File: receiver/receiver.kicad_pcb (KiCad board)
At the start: 4 copper layers, 20.2 x 28 mm, 22 parts, among them J1 CONN_04SCREW, U1 10118194-MICRO-USB, U2 LM3671MF-3.3/NOPBMF05A-M, U3 SN74LVC2T45DCTRE4, U5 FT231XQ-R, U6 MBT3904DW1T1G

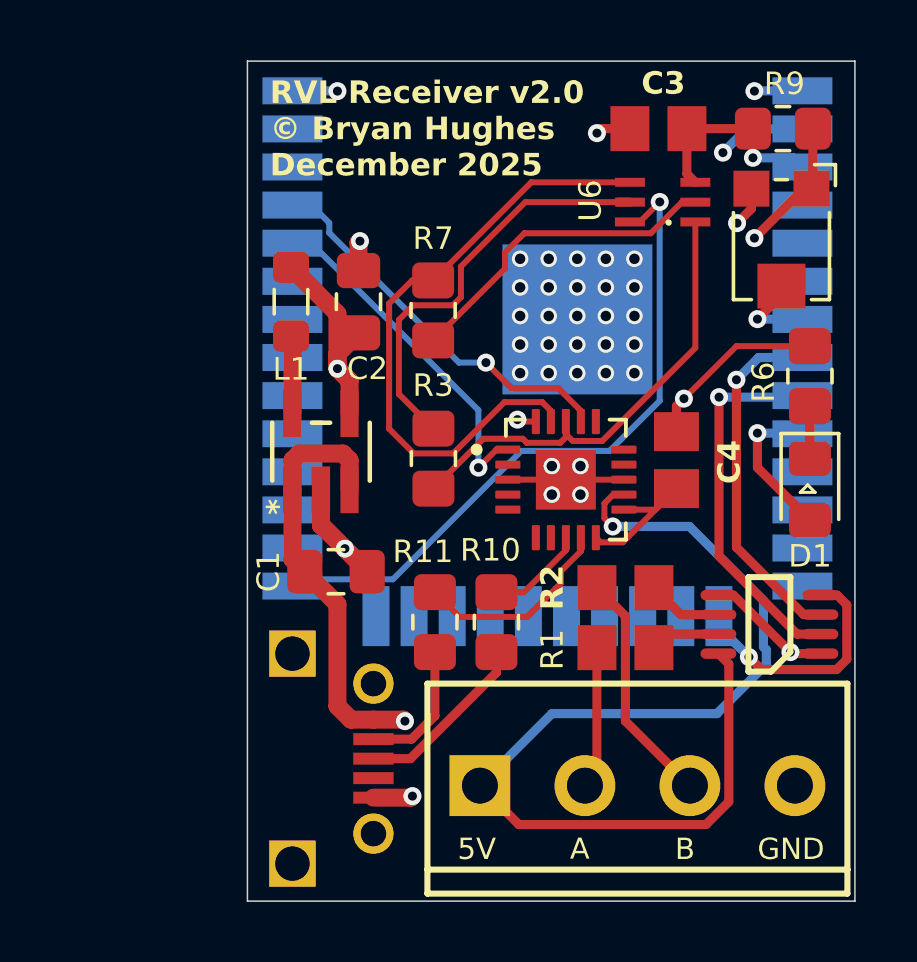
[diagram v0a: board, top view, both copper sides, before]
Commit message: restored v1.7 of receiver, since 2.0 is abandoned
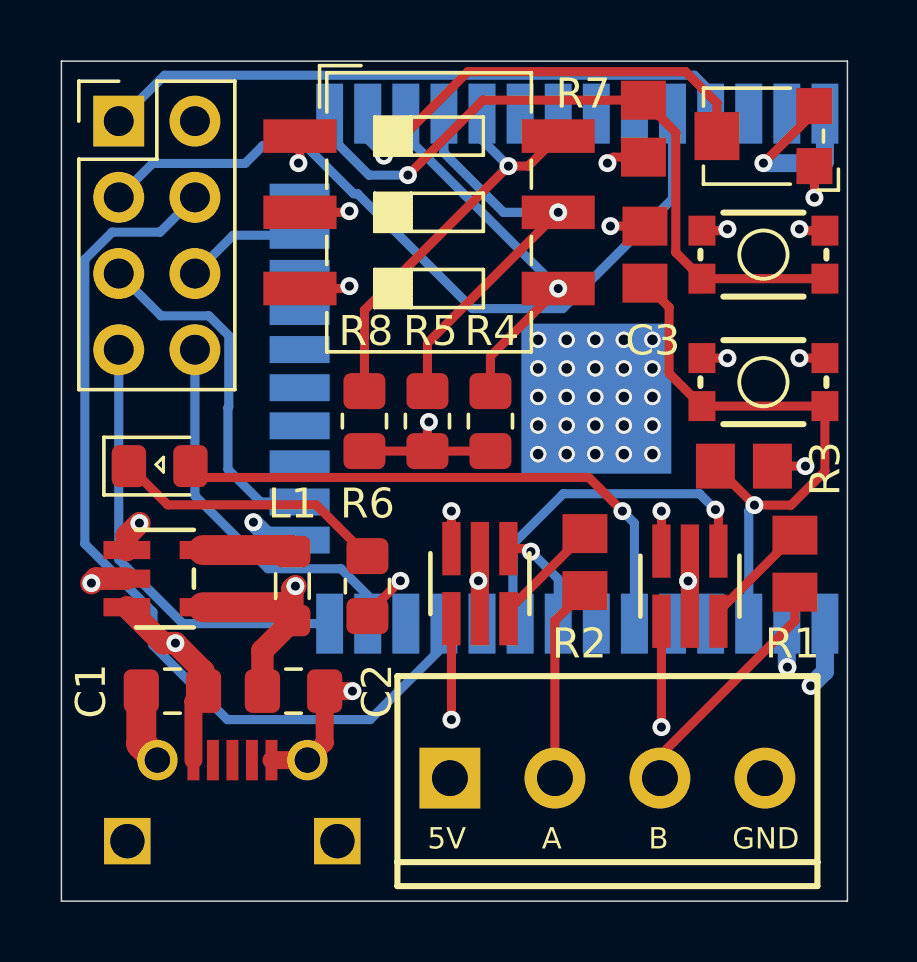
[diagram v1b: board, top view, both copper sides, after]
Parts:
- removed C4: 1uF, receiver:C0805
- removed D1: LED, LED_SMD:LED_0805_2012Metric_Pad1.15x1.40mm_HandSolder
- removed R10, R11: 27, Resistor_SMD:R_0805_2012Metric_Pad1.20x1.40mm_HandSolder
- removed R9: 10k, Resistor_SMD:R_0805_2012Metric_Pad1.20x1.40mm_HandSolder
- removed U5: FT231XQ-R, receiver:QFN50P400X400X80-21N
- removed U6: MBT3904DW1T1G, receiver:SOT236
- added J2: Conn_02x05_Counter_Clockwise, Connector_PinHeader_2.54mm:PinHeader_2x04_P2.54mm_Vertical, F.Cu at (98.7, 116.0)
- added LED1: Power, LED_SMD:LED_0805_2012Metric_Pad1.15x1.40mm_HandSolder, F.Cu at (100.1, 127.5)
- added R4: 10k, Resistor_SMD:R_0805_2012Metric_Pad1.20x1.40mm_HandSolder, F.Cu at (111.1, 126.0)
- added R5: 10k, Resistor_SMD:R_0805_2012Metric_Pad1.20x1.40mm_HandSolder, F.Cu at (109.0, 126.0)
- added R8: 10k, Resistor_SMD:R_0805_2012Metric_Pad1.20x1.40mm_HandSolder, F.Cu at (106.9, 126.0)
- added S2: MOMENTARY-SWITCH-SPST-2-SMD-4.6X2.8MM, receiver:TACTILE_SWITCH_SMD_4.6X2.8MM, F.Cu at (120.2, 120.5)
- added S3: MOMENTARY-SWITCH-SPST-2-SMD-4.6X2.8MM, receiver:TACTILE_SWITCH_SMD_4.6X2.8MM, F.Cu at (120.2, 124.7)
- added SW1: SW_DIP_x03, Button_Switch_SMD:SW_DIP_SPSTx03_Slide_6.7x9.18mm_W8.61mm_P2.54mm_LowProfile, F.Cu at (109.1, 119.0)
- added U4: SN74LVC1T45DBVRDBV6-M, receiver:DBV6-M, F.Cu at (110.8, 131.4)
- R3, R7: footprint Resistor_SMD:R_0805_2012Metric_Pad1.20x1.40mm_HandSolder -> receiver:R0805
- U3: value SN74LVC2T45DCTRE4 -> SN74LVC1T45DBVRDBV6-M; footprint receiver:DCT0008A_L -> receiver:DBV6-M
- moved R6 16.3 mm to (107.0, 131.5), turned to 90 degrees
- moved C2 13.2 mm to (104.5, 135.0), turned to 0 degrees
- moved U$2 13.1 mm to (122.2, 124.2), turned to 90 degrees
- moved R3 10.4 mm to (119.5, 127.5), turned to 0 degrees
- moved L1 9.48 mm to (104.5, 131.5), turned to -90 degrees
- moved R7 9.27 mm to (116.2, 116.2)
- moved C1 6.75 mm to (100.5, 135.0), turned to 180 degrees
- moved U2 6.71 mm to (100.2, 131.2), turned to 0 degrees
- moved R1 6.31 mm to (121.2, 130.8), turned to -90 degrees
- moved C3 4.22 mm to (116.2, 120.5), turned to 90 degrees
- moved RV1 3.62 mm to (120.1, 116.5), turned to 180 degrees
- moved U1 3.40 mm to (102.5, 140.0), turned to 0 degrees
- moved U3 2.94 mm to (117.8, 131.5), turned to 90 degrees
- moved R2 1.60 mm to (114.2, 130.7), turned to -90 degrees
- moved J1 1.03 mm to (109.8, 137.9)
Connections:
- C3 pad 1: EN -> Net-(U$2-EN)
- R1 pad 1: Net-(J1-Pad2) -> Net-(U3-A)
- R1 pad 2: Net-(U3-B1) -> Net-(J1-Pad3)
- R2 pad 1: Net-(J1-Pad3) -> Net-(U4-A)
- R2 pad 2: Net-(U3-B2) -> Net-(J1-Pad2)
- R3 pad 1: Net-(U5-DTR#) -> Net-(U$2-EN)
- R3 pad 2: Net-(R3-Pad2) -> +3.3V
- R7 pad 1: Net-(U5-RTS#) -> Net-(U$2-IO0)
- R7 pad 2: Net-(R7-Pad2) -> +3.3V
- U$2 pad 10: Net-(D1-A) -> unconnected-(U$2-IO25-Pad10)
- U$2 pad 11: unconnected-(U$2-IO26-Pad11) -> GPIO26
- U$2 pad 13: unconnected-(U$2-IO14-Pad13) -> TMS
- U$2 pad 14: unconnected-(U$2-IO12-Pad14) -> TDI
- U$2 pad 16: unconnected-(U$2-IO13-Pad16) -> TCK
- U$2 pad 23: unconnected-(U$2-IO15-Pad23) -> TDO
- U$2 pad 25: IO0 -> Net-(U$2-IO0)
- U$2 pad 26: unconnected-(U$2-IO4-Pad26) -> BRIGHTNESS
- U$2 pad 27: unconnected-(U$2-IO16-Pad27) -> DIP3
- U$2 pad 28: unconnected-(U$2-IO17-Pad28) -> DIP2
- U$2 pad 29: unconnected-(U$2-IO5-Pad29) -> DIP1
- U$2 pad 3: EN -> Net-(U$2-EN)
- U$2 pad 6: unconnected-(U$2-IO34-Pad6) -> Net-(LED1-A)
- U$2 pad 7: BRIGHTNESS -> unconnected-(U$2-IO35-Pad7)
- U1 pad 2: USB_D- -> unconnected-(U1-D--Pad2)
- U1 pad 3: USB_D+ -> unconnected-(U1-D+-Pad3)
- U3 pad 1: +3.3V -> +5V
- U3 pad 2: LED_DATA -> GND
- U3 pad 3: LED_CLOCK -> Net-(U3-A)
- U3 pad 4: GND -> LED_DATA
- U3 pad 5: +3.3V -> GND
- U3 pad 6: Net-(U3-B2) -> +3.3V
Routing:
- net +5V: track 53.0 -> 14.5 mm, vias 2 -> 4
- net GPIO26: track 0.00 -> 30.8 mm
- net Net-(U$2-IO0): track 0.00 -> 23.6 mm, vias 0 -> 1
- net IO0: track 22.7 -> 0.00 mm, vias 1 -> 0
- net Net-(U5-RTS#): track 20.8 -> 0.00 mm
- net Net-(U$2-EN): track 0.00 -> 19.8 mm, vias 0 -> 1
- net Net-(LED1-A): track 0.00 -> 18.9 mm, vias 0 -> 1
- net Net-(U5-DTR#): track 16.3 -> 0.00 mm
- net TDI: track 0.00 -> 14.9 mm
- net Net-(R3-Pad2): track 14.4 -> 0.00 mm
- net RXD: track 11.6 -> 25.8 mm, vias 1 -> 0
- net DIP2: track 0.00 -> 13.7 mm, vias 0 -> 1
- net DIP1: track 0.00 -> 13.7 mm, vias 0 -> 1
- net TMS: track 0.00 -> 12.9 mm
- net BRIGHTNESS: track 2.94 -> 15.4 mm
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- added copper zone on In2.Cu, net +5V
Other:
- board size 20.2 x 28 mm -> 26.2 x 28 mm
- board text added: "RVL Receiver v1.0 © Bryan Hughes January 2025"
- board text removed: "RVL Receiver v2.0 © Bryan Hughes December 2025"
